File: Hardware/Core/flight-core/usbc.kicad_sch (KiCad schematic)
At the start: 4 parts, among them J35 USB_C_Receptacle_USB2.0_16P, U63 USBLC6-2SC6

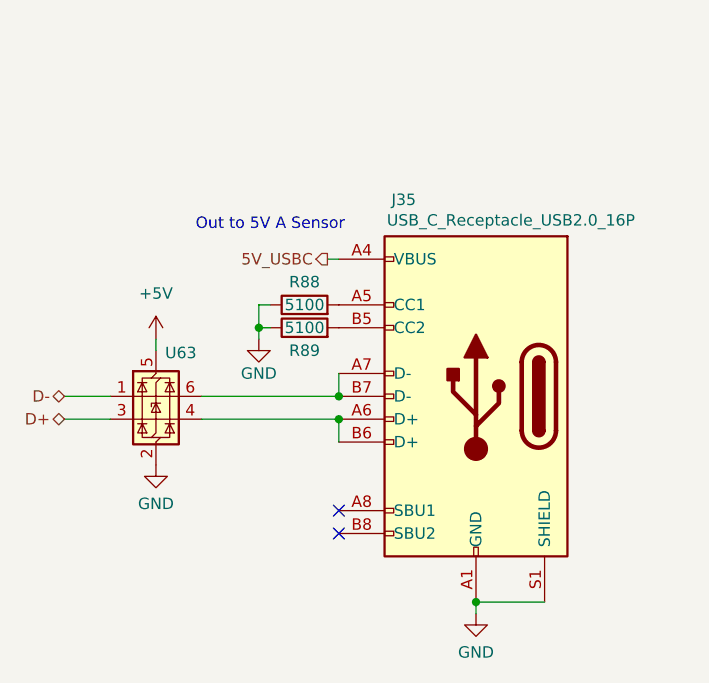
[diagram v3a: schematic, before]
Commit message: added sense pwr cycle pull down, low side cube mosfets, fixed mosi/miso swap on i/o expander, Rs -> generic, reannotated
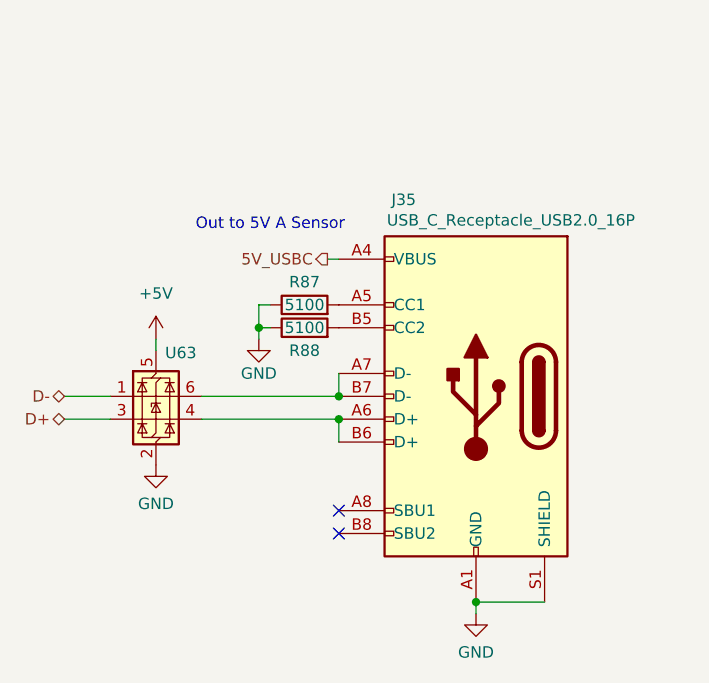
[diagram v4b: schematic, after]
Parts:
- renumbered R88 to R87, R89 to R88
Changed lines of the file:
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@@
 		(on_board yes)
 		(dnp no)
-		(property "Reference" "#PWR0293"
+		(property "Reference" "#PWR0295"
 			(at 134.62 99.06 0)
 			(effects
@@
 			(project "usbc"
 				(path "/93f46f4b-cdf5-47ec-af03-96378e73b2e1/91e18f07-bd3f-4576-bbe1-a0227cf7132e/dc9c6c82-2ca0-4595-949b-0b07300fa078"
-					(reference "#PWR0293")
+					(reference "#PWR0295")
 					(unit 1)
 				)
@@
 		(on_board yes)
 		(dnp no)
-		(property "Reference" "#PWR0294"
+		(property "Reference" "#PWR0296"
 			(at 158.75 129.54 0)
 			(effects
@@
 			(project "usbc"
 				(path "/93f46f4b-cdf5-47ec-af03-96378e73b2e1/91e18f07-bd3f-4576-bbe1-a0227cf7132e/dc9c6c82-2ca0-4595-949b-0b07300fa078"
-					(reference "#PWR0294")
+					(reference "#PWR0296")
 					(unit 1)
 				)
@@
 		(dnp no)
 		(fields_autoplaced yes)
-		(property "Reference" "#PWR0291"
+		(property "Reference" "#PWR0293"
 			(at 123.19 96.52 0)
 			(effects
@@
 			(project "usbc"
 				(path "/93f46f4b-cdf5-47ec-af03-96378e73b2e1/91e18f07-bd3f-4576-bbe1-a0227cf7132e/dc9c6c82-2ca0-4595-949b-0b07300fa078"
-					(reference "#PWR0291")
+					(reference "#PWR0293")
 					(unit 1)
 				)
@@
 		(on_board yes)
 		(dnp no)
-		(property "Reference" "R88"
+		(property "Reference" "R87"
 			(at 139.7 86.36 90)
 			(effects
@@
 			(project ""
 				(path "/93f46f4b-cdf5-47ec-af03-96378e73b2e1/91e18f07-bd3f-4576-bbe1-a0227cf7132e/dc9c6c82-2ca0-4595-949b-0b07300fa078"
-					(reference "R88")
+					(reference "R87")
 					(unit 1)
 				)
@@
 		(on_board yes)
 		(dnp no)
-		(property "Reference" "R89"
+		(property "Reference" "R88"
 			(at 139.7 93.98 90)
 			(effects
@@
 			(project "flight-core"
 				(path "/93f46f4b-cdf5-47ec-af03-96378e73b2e1/91e18f07-bd3f-4576-bbe1-a0227cf7132e/dc9c6c82-2ca0-4595-949b-0b07300fa078"
-					(reference "R89")
+					(reference "R88")
 					(unit 1)
 				)
@@
 		(on_board yes)
 		(dnp no)
-		(property "Reference" "#PWR0292"
+		(property "Reference" "#PWR0294"
 			(at 123.19 113.03 0)
 			(effects
@@
 			(project "usbc"
 				(path "/93f46f4b-cdf5-47ec-af03-96378e73b2e1/91e18f07-bd3f-4576-bbe1-a0227cf7132e/dc9c6c82-2ca0-4595-949b-0b07300fa078"
-					(reference "#PWR0292")
-					(unit 1)
-				)
+					(reference "#PWR0294")
+					(unit 1)
+				)

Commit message: major component area placement begun, installing place footprints plugin, updating connectors to vertical
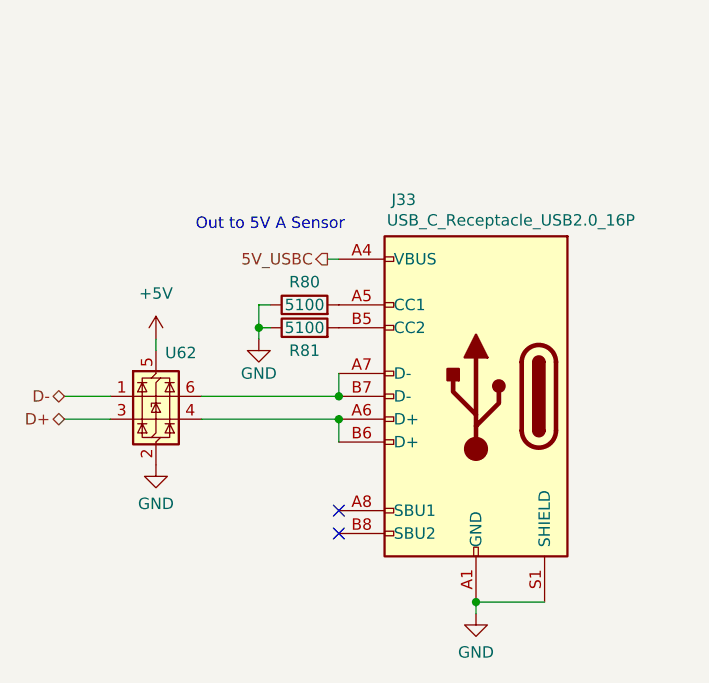
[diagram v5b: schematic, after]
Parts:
- renumbered J35 to J33, R87 to R80, R88 to R81, U63 to U62
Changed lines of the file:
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@@
 		(on_board yes)
 		(dnp no)
-		(property "Reference" "#PWR0295"
+		(property "Reference" "#PWR0283"
 			(at 134.62 99.06 0)
 			(effects
@@
 			(project "usbc"
 				(path "/93f46f4b-cdf5-47ec-af03-96378e73b2e1/91e18f07-bd3f-4576-bbe1-a0227cf7132e/dc9c6c82-2ca0-4595-949b-0b07300fa078"
-					(reference "#PWR0295")
+					(reference "#PWR0283")
 					(unit 1)
 				)
@@
 		(on_board yes)
 		(dnp no)
-		(property "Reference" "U63"
+		(property "Reference" "U62"
 			(at 124.206 94.234 0)
 			(effects
@@
 			(project "usbc"
 				(path "/93f46f4b-cdf5-47ec-af03-96378e73b2e1/91e18f07-bd3f-4576-bbe1-a0227cf7132e/dc9c6c82-2ca0-4595-949b-0b07300fa078"
-					(reference "U63")
+					(reference "U62")
 					(unit 1)
 				)
@@
 		(on_board yes)
 		(dnp no)
-		(property "Reference" "#PWR0296"
+		(property "Reference" "#PWR0284"
 			(at 158.75 129.54 0)
 			(effects
@@
 			(project "usbc"
 				(path "/93f46f4b-cdf5-47ec-af03-96378e73b2e1/91e18f07-bd3f-4576-bbe1-a0227cf7132e/dc9c6c82-2ca0-4595-949b-0b07300fa078"
-					(reference "#PWR0296")
+					(reference "#PWR0284")
 					(unit 1)
 				)
@@
 		(on_board yes)
 		(dnp no)
-		(property "Reference" "J35"
+		(property "Reference" "J33"
 			(at 149.352 77.216 0)
 			(effects
@@
 			(project "usbc"
 				(path "/93f46f4b-cdf5-47ec-af03-96378e73b2e1/91e18f07-bd3f-4576-bbe1-a0227cf7132e/dc9c6c82-2ca0-4595-949b-0b07300fa078"
-					(reference "J35")
+					(reference "J33")
 					(unit 1)
 				)
@@
 		(dnp no)
 		(fields_autoplaced yes)
-		(property "Reference" "#PWR0293"
+		(property "Reference" "#PWR0281"
 			(at 123.19 96.52 0)
 			(effects
@@
 			(project "usbc"
 				(path "/93f46f4b-cdf5-47ec-af03-96378e73b2e1/91e18f07-bd3f-4576-bbe1-a0227cf7132e/dc9c6c82-2ca0-4595-949b-0b07300fa078"
-					(reference "#PWR0293")
+					(reference "#PWR0281")
 					(unit 1)
 				)
@@
 		(on_board yes)
 		(dnp no)
-		(property "Reference" "R87"
+		(property "Reference" "R80"
 			(at 139.7 86.36 90)
 			(effects
@@
 			(project ""
 				(path "/93f46f4b-cdf5-47ec-af03-96378e73b2e1/91e18f07-bd3f-4576-bbe1-a0227cf7132e/dc9c6c82-2ca0-4595-949b-0b07300fa078"
-					(reference "R87")
+					(reference "R80")
 					(unit 1)
 				)
@@
 		(on_board yes)
 		(dnp no)
-		(property "Reference" "R88"
+		(property "Reference" "R81"
 			(at 139.7 93.98 90)
 			(effects
@@
 			(project "flight-core"
 				(path "/93f46f4b-cdf5-47ec-af03-96378e73b2e1/91e18f07-bd3f-4576-bbe1-a0227cf7132e/dc9c6c82-2ca0-4595-949b-0b07300fa078"
-					(reference "R88")
+					(reference "R81")
 					(unit 1)
 				)
@@
 		(on_board yes)
 		(dnp no)
-		(property "Reference" "#PWR0294"
+		(property "Reference" "#PWR0282"
 			(at 123.19 113.03 0)
 			(effects
@@
 			(project "usbc"
 				(path "/93f46f4b-cdf5-47ec-af03-96378e73b2e1/91e18f07-bd3f-4576-bbe1-a0227cf7132e/dc9c6c82-2ca0-4595-949b-0b07300fa078"
-					(reference "#PWR0294")
-					(unit 1)
-				)
+					(reference "#PWR0282")
+					(unit 1)
+				)

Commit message: updated usbc footprint, positioned stm32 peripherals again
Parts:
- J33: footprint Connector_USB:USB_C_Receptacle_G-Switch_GT-USB-7051x -> Connector_USB:USB_C_Receptacle_GCT_USB4105-xx-A_16P_TopMnt_Horizontal
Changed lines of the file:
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@@
 			)
 		)
-		(property "Footprint" "Connector_USB:USB_C_Receptacle_G-Switch_GT-USB-7051x"
+		(property "Footprint" "Connector_USB:USB_C_Receptacle_GCT_USB4105-xx-A_16P_TopMnt_Horizontal"
 			(at 154.94 99.06 0)
 			(effects
